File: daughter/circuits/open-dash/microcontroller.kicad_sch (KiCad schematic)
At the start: 18 parts, among them U10 Temp_Hum_HDC1080DMBR, U9 ESP32-WROOM-32

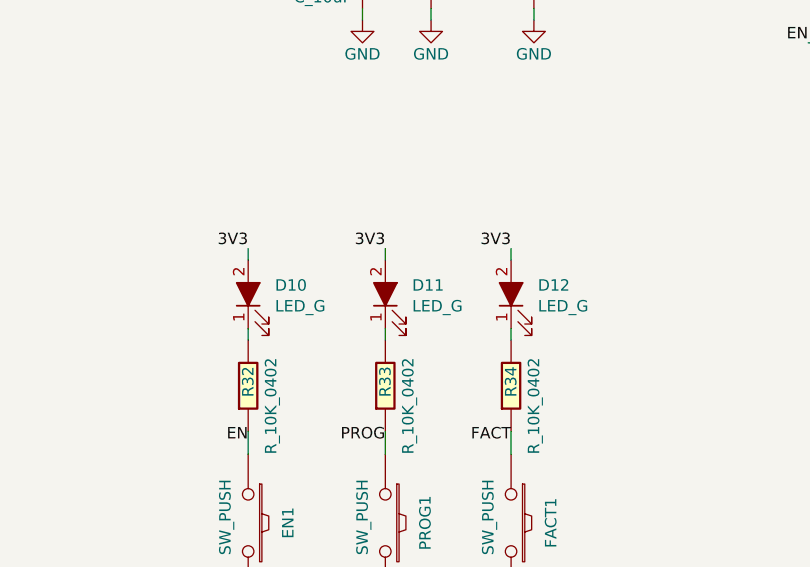
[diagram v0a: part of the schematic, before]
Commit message: Updated hvac circuit
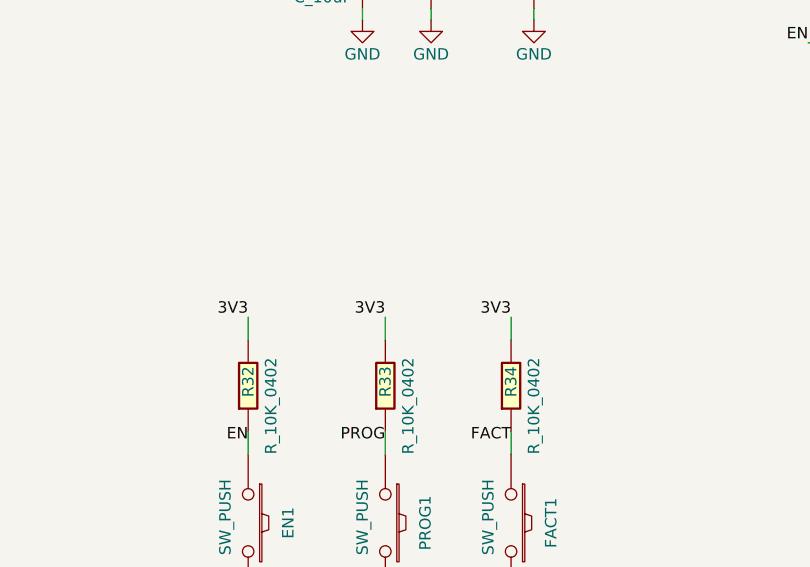
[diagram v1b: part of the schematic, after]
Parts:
- removed D10, D11, D12: LED_G, Diode_SMD:D_0603_1608Metric_Pad1.05x0.95mm_HandSolder, symbol open-dash-daughterboard-rescue:LED_G-Open_Automation
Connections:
- net 3V3: now also R32.2, R33.2, R34.2
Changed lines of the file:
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@@
     (stroke (width 0) (type default) (color 0 0 0 0))
   )
-  (wire (pts (xy 81.28 91.44) (xy 81.28 92.71))
+  (wire (pts (xy 81.28 90.17) (xy 81.28 92.71))
     (stroke (width 0) (type default) (color 0 0 0 0))
   )
@@
     (stroke (width 0) (type default) (color 0 0 0 0))
   )
-  (wire (pts (xy 95.25 82.55) (xy 95.25 83.82))
-    (stroke (width 0) (type default) (color 0 0 0 0))
-  )
   (wire (pts (xy 189.23 118.11) (xy 189.23 119.38))
     (stroke (width 0) (type default) (color 0 0 0 0))
@@
     (stroke (width 0) (type default) (color 0 0 0 0))
   )
-  (wire (pts (xy 81.28 82.55) (xy 81.28 83.82))
-    (stroke (width 0) (type default) (color 0 0 0 0))
-  )
   (wire (pts (xy 161.29 69.85) (xy 160.02 69.85))
     (stroke (width 0) (type default) (color 0 0 0 0))
@@
     (stroke (width 0) (type default) (color 0 0 0 0))
   )
-  (wire (pts (xy 66.04 92.71) (xy 66.04 91.44))
+  (wire (pts (xy 66.04 90.17) (xy 66.04 92.71))
     (stroke (width 0) (type default) (color 0 0 0 0))
   )
@@
     (stroke (width 0) (type default) (color 0 0 0 0))
   )
-  (wire (pts (xy 66.04 82.55) (xy 66.04 83.82))
-    (stroke (width 0) (type default) (color 0 0 0 0))
-  )
   (wire (pts (xy 33.02 59.69) (xy 31.75 59.69))
     (stroke (width 0) (type default) (color 0 0 0 0))
@@
     (stroke (width 0) (type default) (color 0 0 0 0))
   )
-  (wire (pts (xy 95.25 92.71) (xy 95.25 91.44))
+  (wire (pts (xy 95.25 90.17) (xy 95.25 92.71))
     (stroke (width 0) (type default) (color 0 0 0 0))
   )
@@
     (effects (font (size 1.27 1.27)) (justify left bottom))
   )
-  (label "3V3" (at 66.04 82.55 180)
+  (label "3V3" (at 66.04 90.17 180)
     (effects (font (size 1.27 1.27)) (justify right bottom))
   )
@@
     (effects (font (size 1.27 1.27)) (justify left bottom))
   )
-  (label "3V3" (at 81.28 82.55 180)
+  (label "3V3" (at 81.28 90.17 180)
     (effects (font (size 1.27 1.27)) (justify right bottom))
   )
@@
     (effects (font (size 1.27 1.27)) (justify left bottom))
   )
-  (label "3V3" (at 95.25 82.55 180)
+  (label "3V3" (at 95.25 90.17 180)
     (effects (font (size 1.27 1.27)) (justify right bottom))
   )
@@
     (effects (font (size 1.524 1.524)) (justify right))
   )
-  (symbol (lib_id "open-dash-daughterboard-rescue:LED_G-Open_Automation") (at 66.04 87.63 90)
-    (in_bom yes) (on_board yes)
-    (property "Reference" "D10" (id 0) (at 69.0118 86.6394 90)
-      (effects (font (size 1.27 1.27)) (justify right))
-    )
-    (property "Value" "LED_G" (id 1) (at 69.0118 88.9508 90)
-      (effects (font (size 1.27 1.27)) (justify right))
-    )
-    (property "Footprint" "Diode_SMD:D_0603_1608Metric_Pad1.05x0.95mm_HandSolder" (id 2) (at 66.04 87.63 0)
-      (effects (font (size 1.27 1.27)) hide)
-    )
-    (property "Datasheet" "https://datasheet.lcsc.com/szlcsc/Everlight-Elec-19-217-BHC-ZL1M2RY-3T_C72041.pdf" (id 3) (at 66.04 87.63 0)
-      (effects (font (size 1.27 1.27)) hide)
-    )
-    (property "Part Number" "19-217/BHC-ZL1M2RY/3T" (id 4) (at 66.04 87.63 0)
-      (effects (font (size 1.27 1.27)) hide)
-    )
-    (property "LCSC" "C72041" (id 5) (at 153.67 153.67 0)
-      (effects (font (size 1.27 1.27)) hide)
-    )
-    (pin "1")
-    (pin "2")
-  )
-  (symbol (lib_id "open-dash-daughterboard-rescue:LED_G-Open_Automation") (at 81.28 87.63 90)
-    (in_bom yes) (on_board yes)
-    (property "Reference" "D11" (id 0) (at 84.2518 86.6394 90)
-      (effects (font (size 1.27 1.27)) (justify right))
-    )
-    (property "Value" "LED_G" (id 1) (at 84.2518 88.9508 90)
-      (effects (font (size 1.27 1.27)) (justify right))
-    )
-    (property "Footprint" "Diode_SMD:D_0603_1608Metric_Pad1.05x0.95mm_HandSolder" (id 2) (at 81.28 87.63 0)
-      (effects (font (size 1.27 1.27)) hide)
-    )
-    (property "Datasheet" "https://datasheet.lcsc.com/szlcsc/Everlight-Elec-19-217-BHC-ZL1M2RY-3T_C72041.pdf" (id 3) (at 81.28 87.63 0)
-      (effects (font (size 1.27 1.27)) hide)
-    )
-    (property "Part Number" "19-217/BHC-ZL1M2RY/3T" (id 4) (at 81.28 87.63 0)
-      (effects (font (size 1.27 1.27)) hide)
-    )
-    (property "LCSC" "C72041" (id 5) (at 168.91 168.91 0)
-      (effects (font (size 1.27 1.27)) hide)
-    )
-    (pin "1")
-    (pin "2")
-  )
-  (symbol (lib_id "open-dash-daughterboard-rescue:LED_G-Open_Automation") (at 95.25 87.63 90)
-    (in_bom yes) (on_board yes)
-    (property "Reference" "D12" (id 0) (at 98.2218 86.6394 90)
-      (effects (font (size 1.27 1.27)) (justify right))
-    )
-    (property "Value" "LED_G" (id 1) (at 98.2218 88.9508 90)
-      (effects (font (size 1.27 1.27)) (justify right))
-    )
-    (property "Footprint" "Diode_SMD:D_0603_1608Metric_Pad1.05x0.95mm_HandSolder" (id 2) (at 95.25 87.63 0)
-      (effects (font (size 1.27 1.27)) hide)
-    )
-    (property "Datasheet" "https://datasheet.lcsc.com/szlcsc/Everlight-Elec-19-217-BHC-ZL1M2RY-3T_C72041.pdf" (id 3) (at 95.25 87.63 0)
-      (effects (font (size 1.27 1.27)) hide)
-    )
-    (property "Part Number" "19-217/BHC-ZL1M2RY/3T" (id 4) (at 95.25 87.63 0)
-      (effects (font (size 1.27 1.27)) hide)
-    )
-    (property "LCSC" "C72041" (id 5) (at 182.88 182.88 0)
-      (effects (font (size 1.27 1.27)) hide)
-    )
-    (pin "1")
-    (pin "2")
-  )
-  (symbol (lib_id "open-dash-daughterboard-rescue:SW_PUSH-Open_Automation") (at 81.28 113.03 270)
+  (symbol (lib_id "open-dash-daughterboard-rescue:SW_PUSH-Open_Automation") (at 81.28 113.03 270) (unit 1)
     (in_bom yes) (on_board yes)
     (property "Reference" "PROG1" (id 0) (at 85.725 113.03 0))
@@
     (pin "2")
   )
-  (symbol (lib_id "open-dash-daughterboard-rescue:SW_PUSH-Open_Automation") (at 95.25 113.03 270)
+  (symbol (lib_id "open-dash-daughterboard-rescue:SW_PUSH-Open_Automation") (at 95.25 113.03 270) (unit 1)
     (in_bom yes) (on_board yes)
     (property "Reference" "FACT1" (id 0) (at 99.695 113.03 0))
@@
     (pin "2")
   )
-  (symbol (lib_id "open-dash-daughterboard-rescue:SW_PUSH-Open_Automation") (at 66.04 113.03 270)
+  (symbol (lib_id "open-dash-daughterboard-rescue:SW_PUSH-Open_Automation") (at 66.04 113.03 270) (unit 1)
     (in_bom yes) (on_board yes)
     (property "Reference" "EN1" (id 0) (at 70.485 113.03 0))
@@
     (pin "2")
   )
-  (symbol (lib_id "open-dash-daughterboard-rescue:GND-power") (at 195.58 80.01 0)
+  (symbol (lib_id "open-dash-daughterboard-rescue:GND-power") (at 195.58 80.01 0) (unit 1)
     (in_bom yes) (on_board yes)
     (property "Reference" "#PWR079" (id 0) (at 195.58 86.36 0)
@@
     (pin "1")
   )
-  (symbol (lib_id "open-dash-daughterboard-rescue:GND-power") (at 95.25 121.92 0)
+  (symbol (lib_id "open-dash-daughterboard-rescue:GND-power") (at 95.25 121.92 0) (unit 1)
     (in_bom yes) (on_board yes)
     (property "Reference" "#PWR076" (id 0) (at 95.25 128.27 0)
@@
     (pin "1")
   )
-  (symbol (lib_id "open-dash-daughterboard-rescue:GND-power") (at 189.23 119.38 0)
+  (symbol (lib_id "open-dash-daughterboard-rescue:GND-power") (at 189.23 119.38 0) (unit 1)
     (in_bom yes) (on_board yes)
     (property "Reference" "#PWR078" (id 0) (at 189.23 125.73 0)
@@
     (pin "1")
   )
-  (symbol (lib_id "open-dash-daughterboard-rescue:GND-power") (at 212.09 121.92 0)
+  (symbol (lib_id "open-dash-daughterboard-rescue:GND-power") (at 212.09 121.92 0) (unit 1)
     (in_bom yes) (on_board yes)
     (property "Reference" "#PWR080" (id 0) (at 212.09 128.27 0)
@@
     (pin "7")
   )
-  (symbol (lib_id "open-dash-daughterboard-rescue:GND-power") (at 97.79 57.15 0)
+  (symbol (lib_id "open-dash-daughterboard-rescue:GND-power") (at 97.79 57.15 0) (unit 1)
     (in_bom yes) (on_board yes)
     (property "Reference" "#PWR0107" (id 0) (at 97.79 63.5 0)
@@
     (pin "2")
   )
-  (symbol (lib_id "open-dash-daughterboard-rescue:GND-power") (at 86.36 57.15 0)
+  (symbol (lib_id "open-dash-daughterboard-rescue:GND-power") (at 86.36 57.15 0) (unit 1)
     (in_bom yes) (on_board yes)
     (property "Reference" "#PWR075" (id 0) (at 86.36 63.5 0)
@@
     (pin "1")
   )
-  (symbol (lib_id "open-dash-daughterboard-rescue:GND-power") (at 78.74 57.15 0)
+  (symbol (lib_id "open-dash-daughterboard-rescue:GND-power") (at 78.74 57.15 0) (unit 1)
     (in_bom yes) (on_board yes)
     (property "Reference" "#PWR073" (id 0) (at 78.74 63.5 0)
@@
     (pin "9")
   )
-  (symbol (lib_id "open-dash-daughterboard-rescue:GND-power") (at 144.78 127 0)
+  (symbol (lib_id "open-dash-daughterboard-rescue:GND-power") (at 144.78 127 0) (unit 1)
     (in_bom yes) (on_board yes)
     (property "Reference" "#PWR077" (id 0) (at 144.78 133.35 0)
@@
     (pin "1")
   )
-  (symbol (lib_id "open-dash-daughterboard-rescue:GND-power") (at 66.04 121.92 0)
+  (symbol (lib_id "open-dash-daughterboard-rescue:GND-power") (at 66.04 121.92 0) (unit 1)
     (in_bom yes) (on_board yes)
     (property "Reference" "#PWR072" (id 0) (at 66.04 128.27 0)
@@
     (pin "1")
   )
-  (symbol (lib_id "open-dash-daughterboard-rescue:GND-power") (at 81.28 121.92 0)
+  (symbol (lib_id "open-dash-daughterboard-rescue:GND-power") (at 81.28 121.92 0) (unit 1)
     (in_bom yes) (on_board yes)
     (property "Reference" "#PWR074" (id 0) (at 81.28 128.27 0)
